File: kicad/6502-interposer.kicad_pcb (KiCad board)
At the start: 2 copper layers, 68.5 x 43.2 mm, 6 parts, among them J1 Conn_02x16_Odd_Even_MountingP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, J2 Conn_02x16_Odd_Even_MountingP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, J3 Conn_02x09_Odd_Even, U1 65CE02

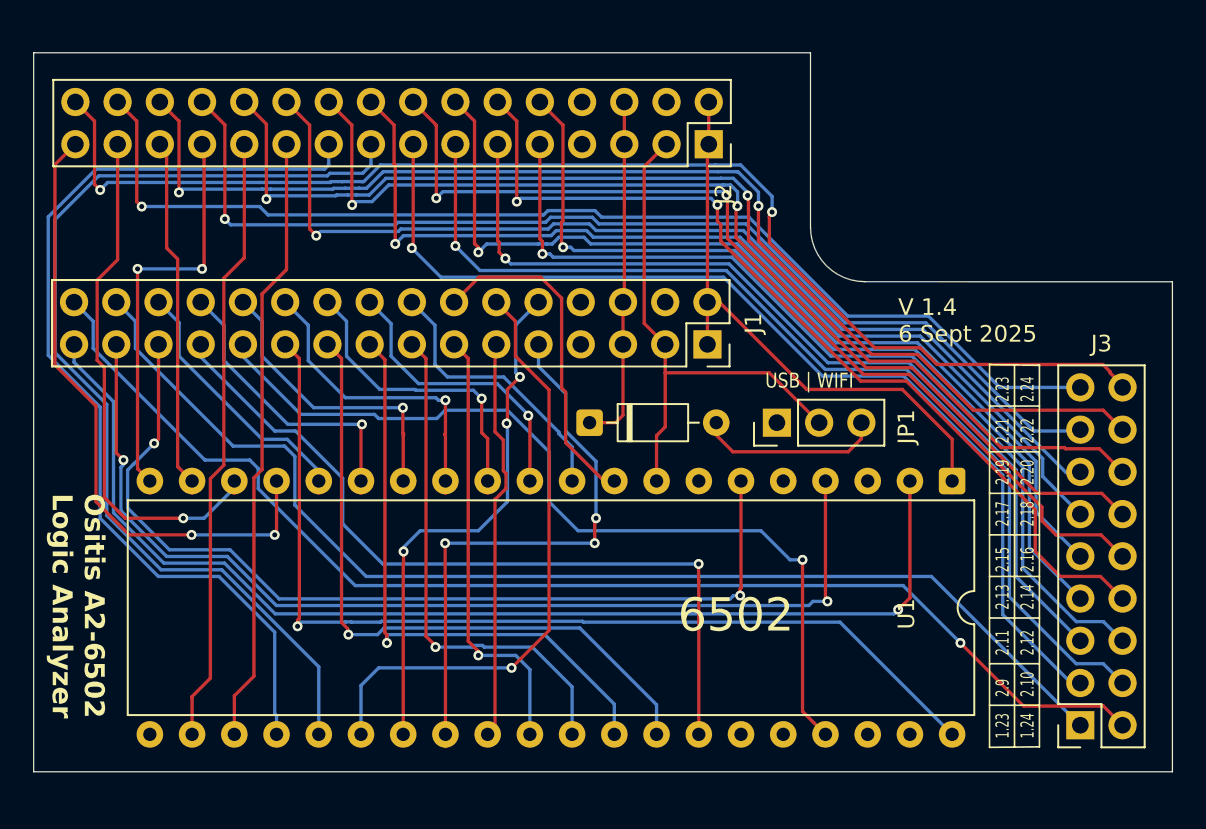
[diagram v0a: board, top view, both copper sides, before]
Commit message: version 1.5
Fix board labelling issues. Fix Numbering issues.
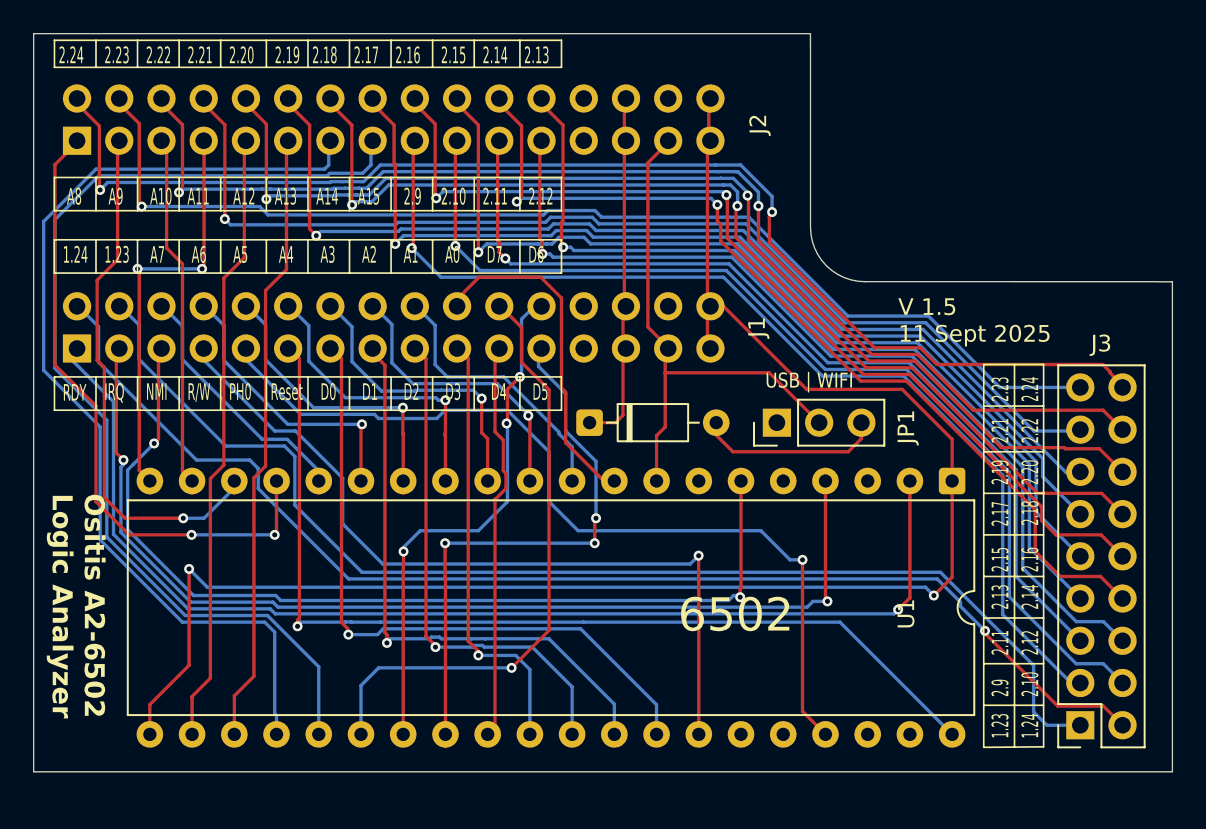
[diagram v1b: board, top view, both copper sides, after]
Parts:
- J1: value Conn_02x16_Odd_Even_MountingPin -> LogicAnalyzer #1; moved to B.Cu
- J2: value Conn_02x16_Odd_Even_MountingPin -> LogicAnalyzer #2; moved to B.Cu
- moved J2 38.0 mm to (47.9, 44.0)
- moved J1 37.9 mm to (47.9, 56.5)
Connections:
- net /Opt18 renamed /Opt2.16
- net /Opt2 renamed /Opt1.2
- net /Opt5 renamed /Opt2.3
- J1 pad 1: GND -> /RDY
- J1 pad 10: /D6 -> /D3
- J1 pad 12: /D7 -> /D5
- J1 pad 13: /D3 -> unconnected-(J1-3V3-Pad13)
- J1 pad 14: /A0 -> /vcc2
- J1 pad 15: /D2 -> +5V
- J1 pad 16: /A1 -> GND
- J1 pad 17: /D1 -> GND
- J1 pad 18: /A2 -> unconnected-(J1-TRG-Pad18)
- J1 pad 19: /D0 -> /vcc2
- J1 pad 2: GND -> /~{IRQ}
- J1 pad 20: /A3 -> unconnected-(J1-3V3-Pad20)
- J1 pad 21: /~{RES} -> /D6
- J1 pad 22: /A4 -> /D7
- J1 pad 23: /ϕ0 -> /A0
- J1 pad 24: /A5 -> /A1
- J1 pad 25: /R/~{W} -> /A2
- J1 pad 26: /A6 -> /A3
- J1 pad 27: /~{NMI} -> /A4
- J1 pad 28: /A7 -> /A5
- J1 pad 29: /~{IRQ} -> /A6
- J1 pad 3: +5V -> /~{NMI}
- J1 pad 30: /Opt1 -> /A7
- J1 pad 31: /RDY -> /Opt1.1
- J1 pad 4: unconnected-(J1-Pin_4-Pad4) -> /R/~{W}
- J1 pad 5: /vcc2 -> /ϕ0
- J1 pad 6: /vcc2 -> /~{RES}
- J1 pad 7: unconnected-(J1-Pin_7-Pad7) -> /D0
- J1 pad 8: unconnected-(J1-Pin_8-Pad8) -> /D1
- J1 pad 9: /D5 -> /D2
- J2 pad 1: GND -> /A8
- J2 pad 10: /Opt7 -> /Opt2.2
- J2 pad 12: /Opt8 -> /Opt2.4
- J2 pad 13: /Opt4 -> unconnected-(J2-3V3-Pad13)
- J2 pad 14: /Opt9 -> /vcc2
- J2 pad 15: /Opt3 -> +5V
- J2 pad 16: /Opt10 -> GND
- J2 pad 18: /Opt11 -> unconnected-(J2-TRG-Pad18)
- J2 pad 19: /A14 -> /vcc2
- J2 pad 2: GND -> /A9
- J2 pad 20: /Opt12 -> unconnected-(J2-3V3-Pad20)
- J2 pad 21: /A13 -> /Opt2.5
- J2 pad 22: /Opt13 -> /Opt2.6
- J2 pad 23: /A12 -> /Opt2.7
- J2 pad 24: /Opt14 -> /Opt2.8
- J2 pad 25: /A11 -> /Opt2.9
- J2 pad 26: /Opt15 -> /Opt2.10
- J2 pad 27: /A10 -> /Opt2.11
- J2 pad 28: /Opt16 -> /Opt2.12
- J2 pad 29: /A9 -> /Opt2.13
- J2 pad 3: +5V -> /A10
- J2 pad 30: /Opt17 -> /Opt2.14
- J2 pad 31: /A8 -> /Opt2.15
- J2 pad 4: unconnected-(J2-Pin_4-Pad4) -> /A11
- J2 pad 5: /vcc2 -> /A12
- J2 pad 6: /vcc2 -> /A13
- J2 pad 7: unconnected-(J2-Pin_7-Pad7) -> /A14
- J2 pad 8: unconnected-(J2-Pin_8-Pad8) -> /A15
- J2 pad 9: /Opt6 -> /Opt2.1
- J3 pad 1: /Opt1 -> /Opt1.1
- J3 pad 10: /Opt10 -> /Opt2.8
- J3 pad 11: /Opt11 -> /Opt2.9
- J3 pad 12: /Opt12 -> /Opt2.10
- J3 pad 13: /Opt13 -> /Opt2.11
- J3 pad 14: /Opt14 -> /Opt2.12
- J3 pad 15: /Opt15 -> /Opt2.13
- J3 pad 16: /Opt16 -> /Opt2.14
- J3 pad 17: /Opt17 -> /Opt2.15
- J3 pad 3: /Opt3 -> /Opt2.1
- J3 pad 4: /Opt4 -> /Opt2.2
- J3 pad 6: /Opt6 -> /Opt2.4
- J3 pad 7: /Opt7 -> /Opt2.5
- J3 pad 8: /Opt8 -> /Opt2.6
- J3 pad 9: /Opt9 -> /Opt2.7
- U1 pad 21: (no net) -> GND
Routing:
- net /Opt1.1: track 0.00 -> 73.1 mm
- net /Opt2.14: track 0.00 -> 71.5 mm, vias 0 -> 2
- net /Opt16: track 71.4 -> 0.00 mm, vias 2 -> 0
- net /Opt1: track 71.2 -> 0.00 mm
- net /Opt17: track 68.9 -> 0.00 mm, vias 1 -> 0
- net /Opt2.15: track 0.00 -> 68.9 mm, vias 0 -> 1
- net /Opt2.12: track 0.00 -> 67.4 mm, vias 0 -> 2
- net /Opt14: track 67.4 -> 0.00 mm, vias 2 -> 0
- net /Opt2.13: track 0.00 -> 64.8 mm, vias 0 -> 1
- net /Opt15: track 64.8 -> 0.00 mm, vias 1 -> 0
- net GND: track 35.6 -> 99.3 mm, vias 0 -> 2
- net /Opt2.10: track 0.00 -> 63.2 mm, vias 0 -> 2
- net /Opt12: track 63.2 -> 0.00 mm, vias 2 -> 0
- net /Opt3: track 62.1 -> 0.00 mm, vias 1 -> 0
- net /Opt2.1: track 0.00 -> 62.1 mm, vias 0 -> 1
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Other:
- board size 68.5 x 43.2 mm -> 68.5 x 44.4 mm
- board text added: "A0"
- board text added: "A1"
- board text added: "A10"
- board text added: "A11"
- board text added: "A12"
- board text added: "A13"
- board text added: "A14"
- board text added: "A15"
- board text added: "A2"
- board text added: "A3"
- board text added: "A4"
- board text added: "A5"
- board text added: "A6"
- board text added: "A7"
- board text added: "A8"
- board text added: "A9"
- board text added: "D0"
- board text added: "D2"
- board text added: "D3"
- board text added: "D4"
- board text added: "D5"
- board text added: "D6"
- board text added: "D7"
- board text added: "IRQ"
- board text added: "NMI"
- board text added: "PH0"
- board text added: "R/W"
- board text added: "RDY"
- board text added: "Reset"
- board text added: "V 1.5 11 Sept 2025"
- board text removed: "V 1.4 6 Sept 2025"

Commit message: updates for v1.5
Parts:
- J1, J2: moved to F.Cu
- moved J1 2.95 mm to (47.6, 53.6), turned to 90 degrees
- moved J2 2.45 mm to (47.7, 41.6), turned to 90 degrees
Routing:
- net /A11: track 25.5 -> 24.6 mm

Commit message: final cleanup
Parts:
- added G***: LOGO, OsitisLib:ois-logo-sm, B.Cu at (74.2, 72.2)

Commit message: Added Phase1 and SYNC
Ended up digging into the 6502 documentation to understand why SYNC and Phase1 are important. Although the IIc and IIe do not use these signals, they do have a function. Sync tells us when the cpu is executing an action, on the system. Phase1 is the inverse of Phase0 or Phase2, and is the time when the Apple II series performs memory actions. Video phase addressing traffic is not visible to the CPU in the Apple II series, the Option ports need to be used to grab those signals. RAn
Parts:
- J3: value Conn_02x09_Odd_Even -> Conn_02x08_Odd_Even; footprint Connector_PinSocket_2.54mm:PinSocket_2x09_P2.54mm_Vertical -> Connector_PinSocket_2.54mm:PinSocket_2x08_P2.54mm_Vertical
- moved JP1 1.71 mm to (91.7, 61.0)
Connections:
- J1 pad 31: /Opt1.1 -> /SYNC
- J1 pad 32: /Opt1.2 -> /ϕ1
- J3 pad 1: /Opt1.1 -> /Opt2.1
- J3 pad 10: /Opt2.8 -> /Opt2.10
- J3 pad 11: /Opt2.9 -> /Opt2.11
- J3 pad 12: /Opt2.10 -> /Opt2.12
- J3 pad 13: /Opt2.11 -> /Opt2.13
- J3 pad 14: /Opt2.12 -> /Opt2.14
- J3 pad 15: /Opt2.13 -> /Opt2.15
- J3 pad 16: /Opt2.14 -> /Opt2.16
- J3 pad 2: /Opt1.2 -> /Opt2.2
- J3 pad 3: /Opt2.1 -> /Opt2.3
- J3 pad 4: /Opt2.2 -> /Opt2.4
- J3 pad 5: /Opt2.3 -> /Opt2.5
- J3 pad 6: /Opt2.4 -> /Opt2.6
- J3 pad 7: /Opt2.5 -> /Opt2.7
- J3 pad 8: /Opt2.6 -> /Opt2.8
- J3 pad 9: /Opt2.7 -> /Opt2.9
- U1 pad 3: unconnected-(U1-ϕ1-Pad3) -> /ϕ1
- U1 pad 7: unconnected-(U1-SYNC-Pad7) -> /SYNC
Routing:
- net /Opt1.2: track 75.8 -> 0.00 mm, vias 1 -> 0
- net /Opt1.1: track 73.1 -> 0.00 mm
- net /ϕ1: track 0.00 -> 62.0 mm, vias 0 -> 1
- net /SYNC: track 0.00 -> 51.4 mm, vias 0 -> 1
- net /Opt2.2: track 61.5 -> 66.2 mm
- net /Opt2.1: track 62.1 -> 66.3 mm
- net /Opt2.3: track 54.9 -> 59.0 mm
- net /Opt2.4: track 54.8 -> 58.7 mm
- net /Opt2.5: track 52.2 -> 55.8 mm
- net /Opt2.9: track 58.4 -> 61.9 mm
- net /Opt2.7: track 55.9 -> 59.4 mm
- net /Opt2.6: track 55.7 -> 58.5 mm
- net /Opt2.8: track 58.9 -> 61.5 mm
- net /Opt2.11: track 61.2 -> 63.8 mm
- net +5V: track 32.9 -> 35.4 mm
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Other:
- board text added: "PH1"
- board text added: "SYNC"
- board text added: "V 1.5 22 Sept 2025 https://github.com/eositis/a2-6502-analyzer"
- board text removed: "1.23"
- board text removed: "1.24"
- board text removed: "V 1.5 11 Sept 2025"

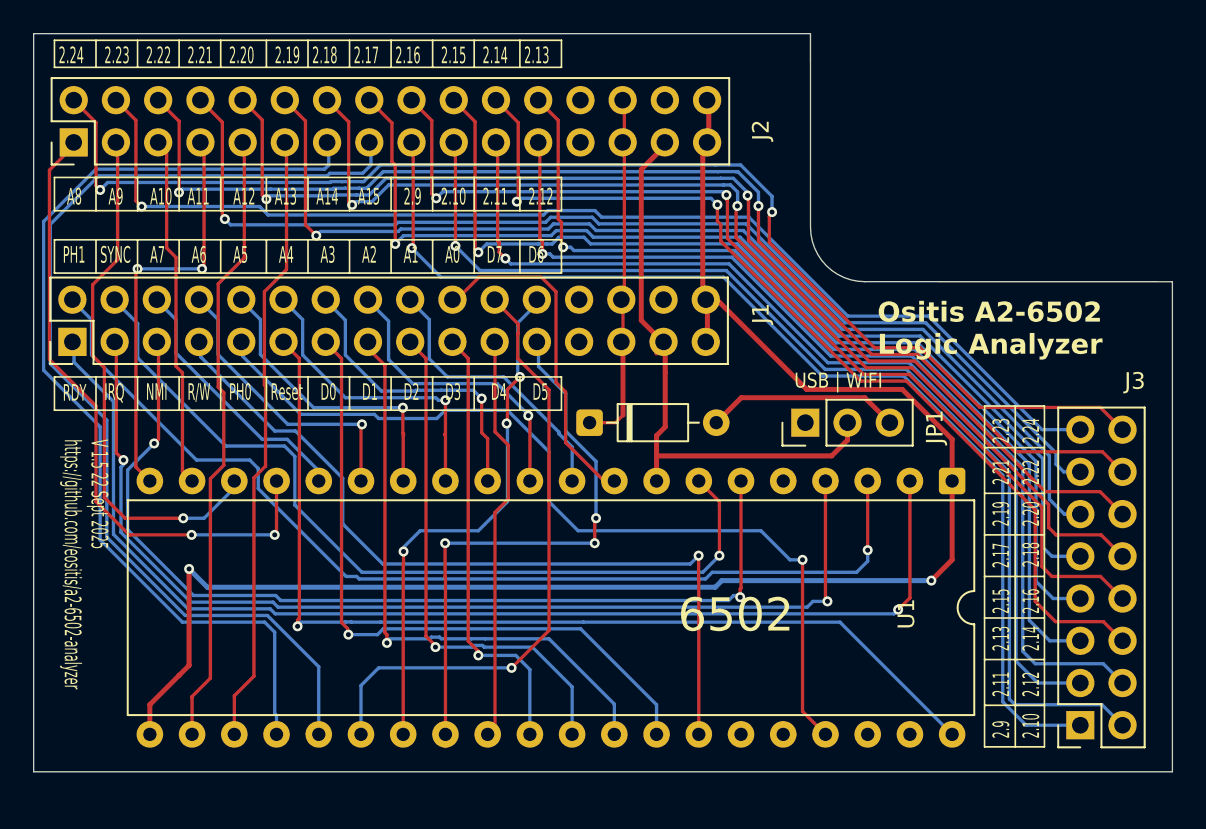
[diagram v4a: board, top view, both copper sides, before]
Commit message: fixed labels, sync routing
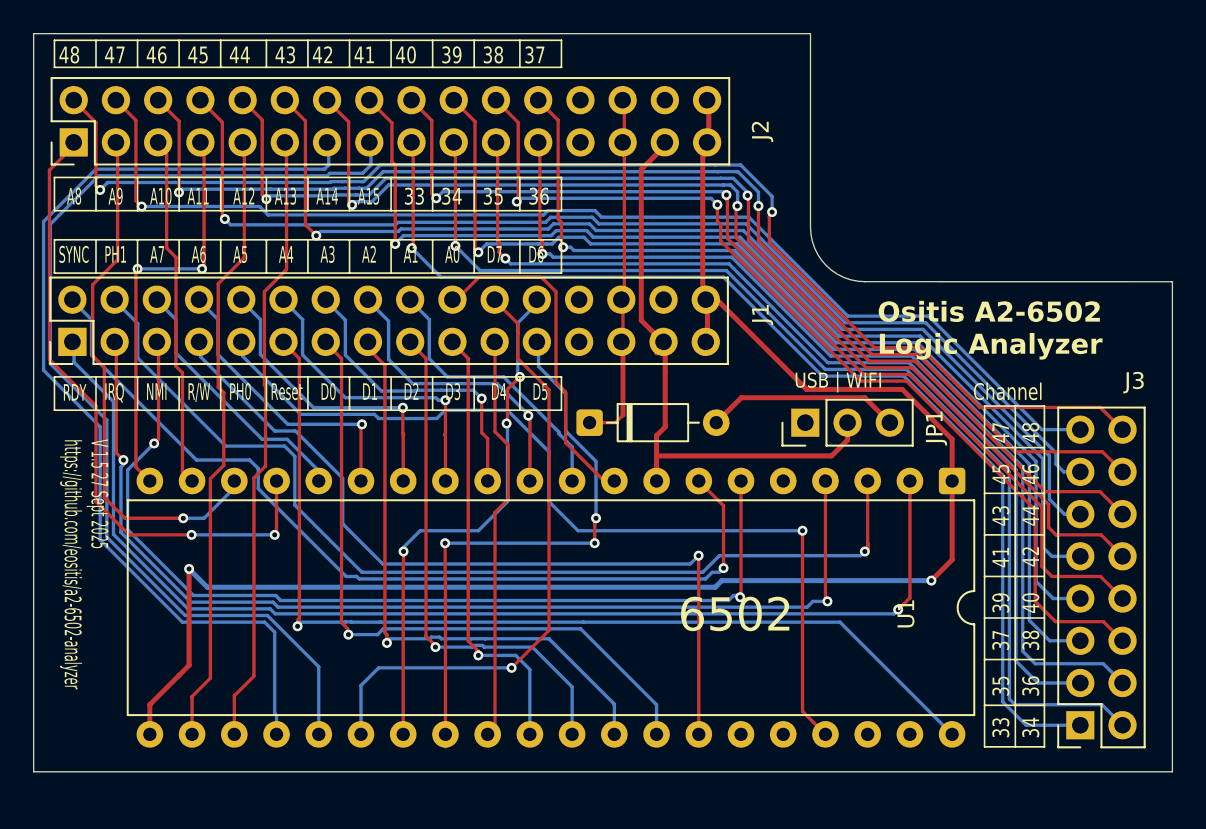
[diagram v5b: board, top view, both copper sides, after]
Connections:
- net /Opt2.1 renamed /CH-33
- net /Opt2.10 renamed /CH-42
- net /Opt2.11 renamed /CH-43
- net /Opt2.12 renamed /CH-44
- net /Opt2.13 renamed /CH-45
- net /Opt2.14 renamed /CH-46
- net /Opt2.15 renamed /CH-47
- net /Opt2.16 renamed /CH-48
- net /Opt2.2 renamed /CH-34
- net /Opt2.3 renamed /CH-35
- net /Opt2.4 renamed /CH-36
- net /Opt2.5 renamed /CH-37
- net /Opt2.6 renamed /CH-38
- net /Opt2.7 renamed /CH-39
- net /Opt2.8 renamed /CH-40
- net /Opt2.9 renamed /CH-41
- J1 pad 31: /SYNC -> /ϕ1
- J1 pad 32: /ϕ1 -> /SYNC
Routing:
- net /SYNC: track 51.4 -> 54.0 mm
- net /ϕ1: track 62.0 -> 59.9 mm
- net /ϕ0: track 52.7 -> 53.7 mm
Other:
- board text added: "33"
- board text added: "34"
- board text added: "35"
- board text added: "36"
- board text added: "37"
- board text added: "38"
- board text added: "39"
- board text added: "40"
- board text added: "41"
- board text added: "42"
- board text added: "43"
- board text added: "44"
- board text added: "45"
- board text added: "46"
- board text added: "47"
- board text added: "48"
- board text added: "Channel"
- board text added: "V 1.5 27 Sept 2025 https://github.com/eositis/a2-6502-analyzer"
- board text removed: "2.10"
- board text removed: "2.11"
- board text removed: "2.12"
- board text removed: "2.13"
- board text removed: "2.14"
- board text removed: "2.15"
- board text removed: "2.16"
- board text removed: "2.17"
- board text removed: "2.18"
- board text removed: "2.19"
- board text removed: "2.20"
- board text removed: "2.21"
- board text removed: "2.22"
- board text removed: "2.23"
- board text removed: "2.24"
- board text removed: "2.9"
- board text removed: "V 1.5 22 Sept 2025 https://github.com/eositis/a2-6502-analyzer"
